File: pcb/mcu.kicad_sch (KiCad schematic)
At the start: 6 parts, among them U1 STM32G0B1RET6

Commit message: fix CAN tx/rx/stb, remove unused SWO
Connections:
- net RX: now also U1.51 (PD1); no longer U1.41 (PD9)
- net STB: now also U1.52 (PD2)
- net TX: now also U1.50 (PD0); no longer U1.40 (PD8)
- net MCU_STATUS_LED: now reaches U1.13 (PC0)
- no-connect marks 38 -> 37
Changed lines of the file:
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@@
+	)
+	(no_connect
+		(at 137.16 104.14)
 	)
 	(no_connect
@@
 	)
 	(no_connect
-		(at 81.28 106.68)
-	)
-	(no_connect
 		(at 137.16 129.54)
 	)
@@
 	(no_connect
 		(at 137.16 121.92)
-	)
-	(no_connect
-		(at 81.28 86.36)
 	)
 	(no_connect
@@
 	)
 	(bus_entry
+		(at 44.45 83.82)
+		(size 2.54 2.54)
+		(stroke
+			(width 0)
+			(type default)
+		)
+	)
+	(bus_entry
 		(at 191.77 62.23)
 		(size -2.54 2.54)
@@
 	)
 	(bus_entry
-		(at 53.34 95.25)
-		(size 2.54 2.54)
-		(stroke
-			(width 0)
-			(type default)
-		)
-	)
-	(bus_entry
-		(at 53.34 105.41)
-		(size 2.54 2.54)
-		(stroke
-			(width 0)
-			(type default)
-		)
-	)
-	(bus_entry
 		(at 191.77 69.85)
 		(size -2.54 2.54)
@@
 	)
 	(bus_entry
-		(at 53.34 97.79)
+		(at 44.45 81.28)
 		(size 2.54 2.54)
 		(stroke
@@
 		)
 	)
+	(bus_entry
+		(at 44.45 78.74)
+		(size 2.54 2.54)
+		(stroke
+			(width 0)
+			(type default)
+		)
+	)
 	(wire
 		(pts
@@
 	(wire
 		(pts
+			(xy 77.47 106.68) (xy 81.28 106.68)
+		)
+		(stroke
+			(width 0)
+			(type default)
+		)
+	)
+	(bus
+		(pts
+			(xy 44.45 81.28) (xy 44.45 83.82)
+		)
+		(stroke
+			(width 0)
+			(type default)
+		)
+	)
+	(bus
+		(pts
+			(xy 44.45 68.58) (xy 44.45 78.74)
+		)
+		(stroke
+			(width 0)
+			(type default)
+		)
+	)
+	(wire
+		(pts
 			(xy 137.16 66.04) (xy 156.21 66.04)
 		)
@@
 	(wire
 		(pts
-			(xy 76.2 101.6) (xy 81.28 101.6)
-		)
-		(stroke
-			(width 0)
-			(type default)
-		)
-	)
-	(wire
-		(pts
 			(xy 55.88 116.84) (xy 81.28 116.84)
 		)
@@
 	(wire
 		(pts
+			(xy 46.99 81.28) (xy 81.28 81.28)
+		)
+		(stroke
+			(width 0)
+			(type default)
+		)
+	)
+	(wire
+		(pts
 			(xy 172.72 67.31) (xy 189.23 67.31)
 		)
@@
 		)
 	)
-	(bus
-		(pts
-			(xy 53.34 85.09) (xy 53.34 95.25)
-		)
-		(stroke
-			(width 0)
-			(type default)
-		)
-	)
-	(wire
-		(pts
-			(xy 76.2 97.79) (xy 77.47 99.06)
-		)
-		(stroke
-			(width 0)
-			(type default)
-		)
-	)
 	(wire
 		(pts
@@
 	(wire
 		(pts
-			(xy 55.88 97.79) (xy 76.2 97.79)
-		)
-		(stroke
-			(width 0)
-			(type default)
-		)
-	)
-	(bus
-		(pts
-			(xy 53.34 95.25) (xy 53.34 97.79)
-		)
-		(stroke
-			(width 0)
-			(type default)
-		)
-	)
-	(wire
-		(pts
 			(xy 137.16 76.2) (xy 156.21 76.2)
 		)
@@
 		)
 	)
-	(wire
-		(pts
-			(xy 77.47 99.06) (xy 81.28 99.06)
-		)
-		(stroke
-			(width 0)
-			(type default)
-		)
-	)
 	(bus
 		(pts
@@
 	(wire
 		(pts
+			(xy 46.99 86.36) (xy 81.28 86.36)
+		)
+		(stroke
+			(width 0)
+			(type default)
+		)
+	)
+	(wire
+		(pts
 			(xy 151.13 88.9) (xy 153.67 91.44)
 		)
@@
 		)
 	)
-	(wire
-		(pts
-			(xy 55.88 107.95) (xy 62.23 107.95)
+	(bus
+		(pts
+			(xy 44.45 78.74) (xy 44.45 81.28)
 		)
 		(stroke
@@
 	(wire
 		(pts
-			(xy 74.93 100.33) (xy 76.2 101.6)
-		)
-		(stroke
-			(width 0)
-			(type default)
-		)
-	)
-	(wire
-		(pts
 			(xy 87.63 50.8) (xy 92.71 50.8)
 		)
@@
 	(wire
 		(pts
+			(xy 46.99 83.82) (xy 81.28 83.82)
+		)
+		(stroke
+			(width 0)
+			(type default)
+		)
+	)
+	(wire
+		(pts
 			(xy 139.7 101.6) (xy 137.16 101.6)
 		)
@@
 	(bus
 		(pts
-			(xy 53.34 97.79) (xy 53.34 105.41)
-		)
-		(stroke
-			(width 0)
-			(type default)
-		)
-	)
-	(bus
-		(pts
 			(xy 165.1 87.63) (xy 165.1 88.9)
-		)
-		(stroke
-			(width 0)
-			(type default)
-		)
-	)
-	(wire
-		(pts
-			(xy 55.88 100.33) (xy 74.93 100.33)
 		)
 		(stroke
@@
 		)
 	)
+	(label "STB"
+		(at 46.99 86.36 0)
+		(effects
+			(font
+				(size 1.27 1.27)
+			)
+			(justify left bottom)
+		)
+	)
 	(label "DBG_UART.RX"
 		(at 161.29 137.16 180)
@@
 		)
 	)
+	(label "RX"
+		(at 46.99 83.82 0)
+		(effects
+			(font
+				(size 1.27 1.27)
+			)
+			(justify left bottom)
+		)
+	)
 	(label "HLINE.RX"
 		(at 172.72 83.82 0)
@@
 		)
 	)
-	(label "STB"
-		(at 55.88 107.95 0)
-		(effects
-			(font
-				(size 1.27 1.27)
-			)
-			(justify left bottom)
-		)
-	)
-	(label "TX"
-		(at 55.88 97.79 0)
-		(effects
-			(font
-				(size 1.27 1.27)
-			)
-			(justify left bottom)
-		)
-	)
 	(label "KLINE.TX"
 		(at 67.31 116.84 180)
@@
 		)
 	)
-	(label "RX"
-		(at 55.88 100.33 0)
+	(label "TX"
+		(at 46.99 81.28 0)
 		(effects
 			(font
@@
 		)
 	)
-	(hierarchical_label "MCU_SWO"
+	(hierarchical_label "MCU_STATUS_LED"
 		(shape output)
-		(at 139.7 104.14 0)
+		(at 77.47 106.68 180)
+		(effects
+			(font
+				(size 1.27 1.27)
+			)
+			(justify right)
+		)
+	)
+	(hierarchical_label "{CAN_MCU}"
+		(shape bidirectional)
+		(at 44.45 68.58 0)
 		(effects
 			(font
@@
 		)
 	)
-	(hierarchical_label "{CAN_MCU}"
-		(shape bidirectional)
-		(at 53.34 85.09 0)
-		(effects
-			(font
-				(size 1.27 1.27)
-			)
-			(justify left)
-		)
-	)

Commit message: status/info leds, extra 5v cap
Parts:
- renumbered C9 to C20, C10 to C21, C11 to C22, C12 to C23
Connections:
- net MCU_LED_DRV: now reaches U1.38 (PC6)
- no-connect marks 37 -> 38
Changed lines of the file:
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@@
-	)
-	(no_connect
-		(at 81.28 121.92)
 	)
 	(no_connect
@@
 	)
 	(no_connect
+		(at 81.28 101.6)
+	)
+	(no_connect
 		(at 81.28 93.98)
 	)
@@
 	(no_connect
 		(at 137.16 127)
+	)
+	(no_connect
+		(at 81.28 99.06)
 	)
 	(no_connect
@@
 		)
 	)
+	(wire
+		(pts
+			(xy 73.66 121.92) (xy 81.28 121.92)
+		)
+		(stroke
+			(width 0)
+			(type default)
+		)
+	)
 	(bus
 		(pts
@@
 		(shape input)
 		(at 67.31 76.2 180)
+		(effects
+			(font
+				(size 1.27 1.27)
+			)
+			(justify right)
+		)
+	)
+	(hierarchical_label "MCU_LED_DRV"
+		(shape output)
+		(at 73.66 121.92 180)
 		(effects
 			(font
@@
 		(on_board yes)
 		(dnp no)
-		(property "Reference" "C12"
+		(property "Reference" "C23"
 			(at 94.488 52.324 0)
 			(effects
@@
 			(project "kh_obd2_interface"
 				(path "/0736e313-8db4-41af-b70d-53af7104d2ca/c18d60e7-bd36-4ea9-b2f1-adbb43a4c5ec"
-					(reference "C12")
+					(reference "C23")
 					(unit 1)
 				)
@@
 		(on_board yes)
 		(dnp no)
-		(property "Reference" "C10"
+		(property "Reference" "C21"
 			(at 127.508 52.324 0)
 			(effects
@@
 			(project "kh_obd2_interface"
 				(path "/0736e313-8db4-41af-b70d-53af7104d2ca/c18d60e7-bd36-4ea9-b2f1-adbb43a4c5ec"
-					(reference "C10")
+					(reference "C21")
 					(unit 1)
 				)
@@
 		(on_board yes)
 		(dnp no)
-		(property "Reference" "C11"
+		(property "Reference" "C22"
 			(at 84.328 52.324 0)
 			(effects
@@
 			(project ""
 				(path "/0736e313-8db4-41af-b70d-53af7104d2ca/c18d60e7-bd36-4ea9-b2f1-adbb43a4c5ec"
-					(reference "C11")
+					(reference "C22")
 					(unit 1)
 				)
@@
 		(on_board yes)
 		(dnp no)
-		(property "Reference" "C9"
+		(property "Reference" "C20"
 			(at 117.348 52.324 0)
 			(effects
@@
 			(project ""
 				(path "/0736e313-8db4-41af-b70d-53af7104d2ca/c18d60e7-bd36-4ea9-b2f1-adbb43a4c5ec"
-					(reference "C9")
+					(reference "C20")
 					(unit 1)
 				)

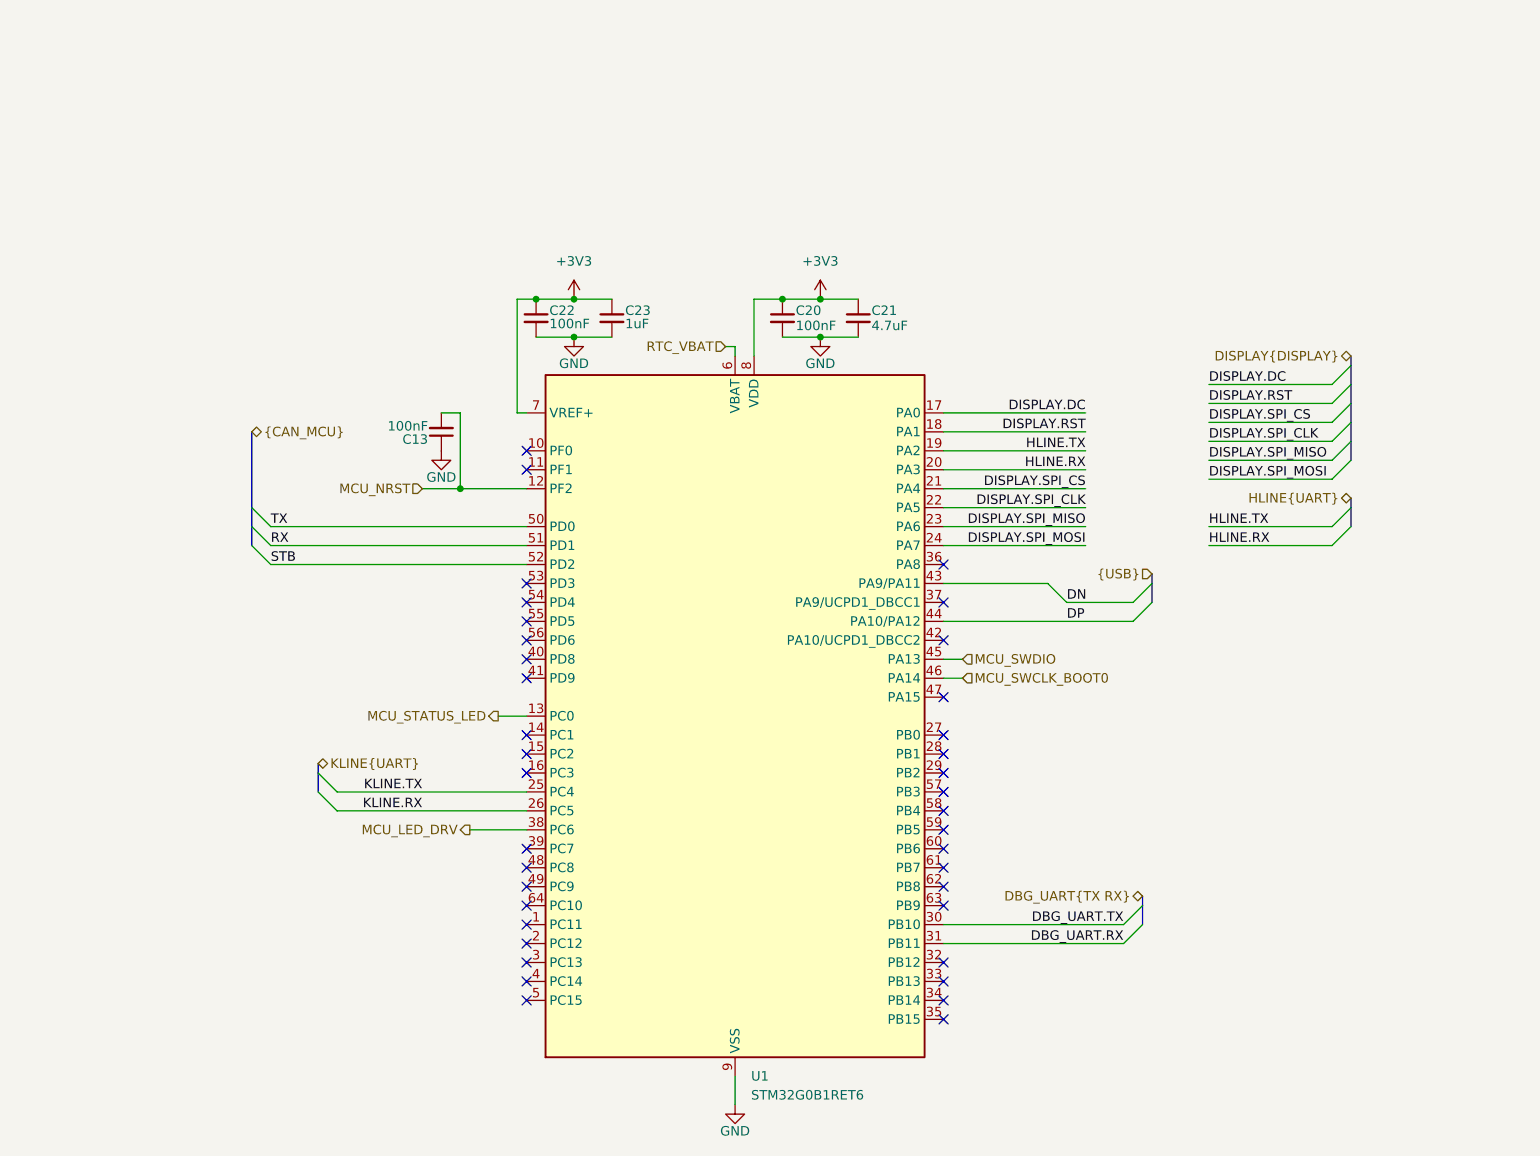
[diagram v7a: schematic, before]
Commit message: dbg uart, nrst, SCS drive, etc
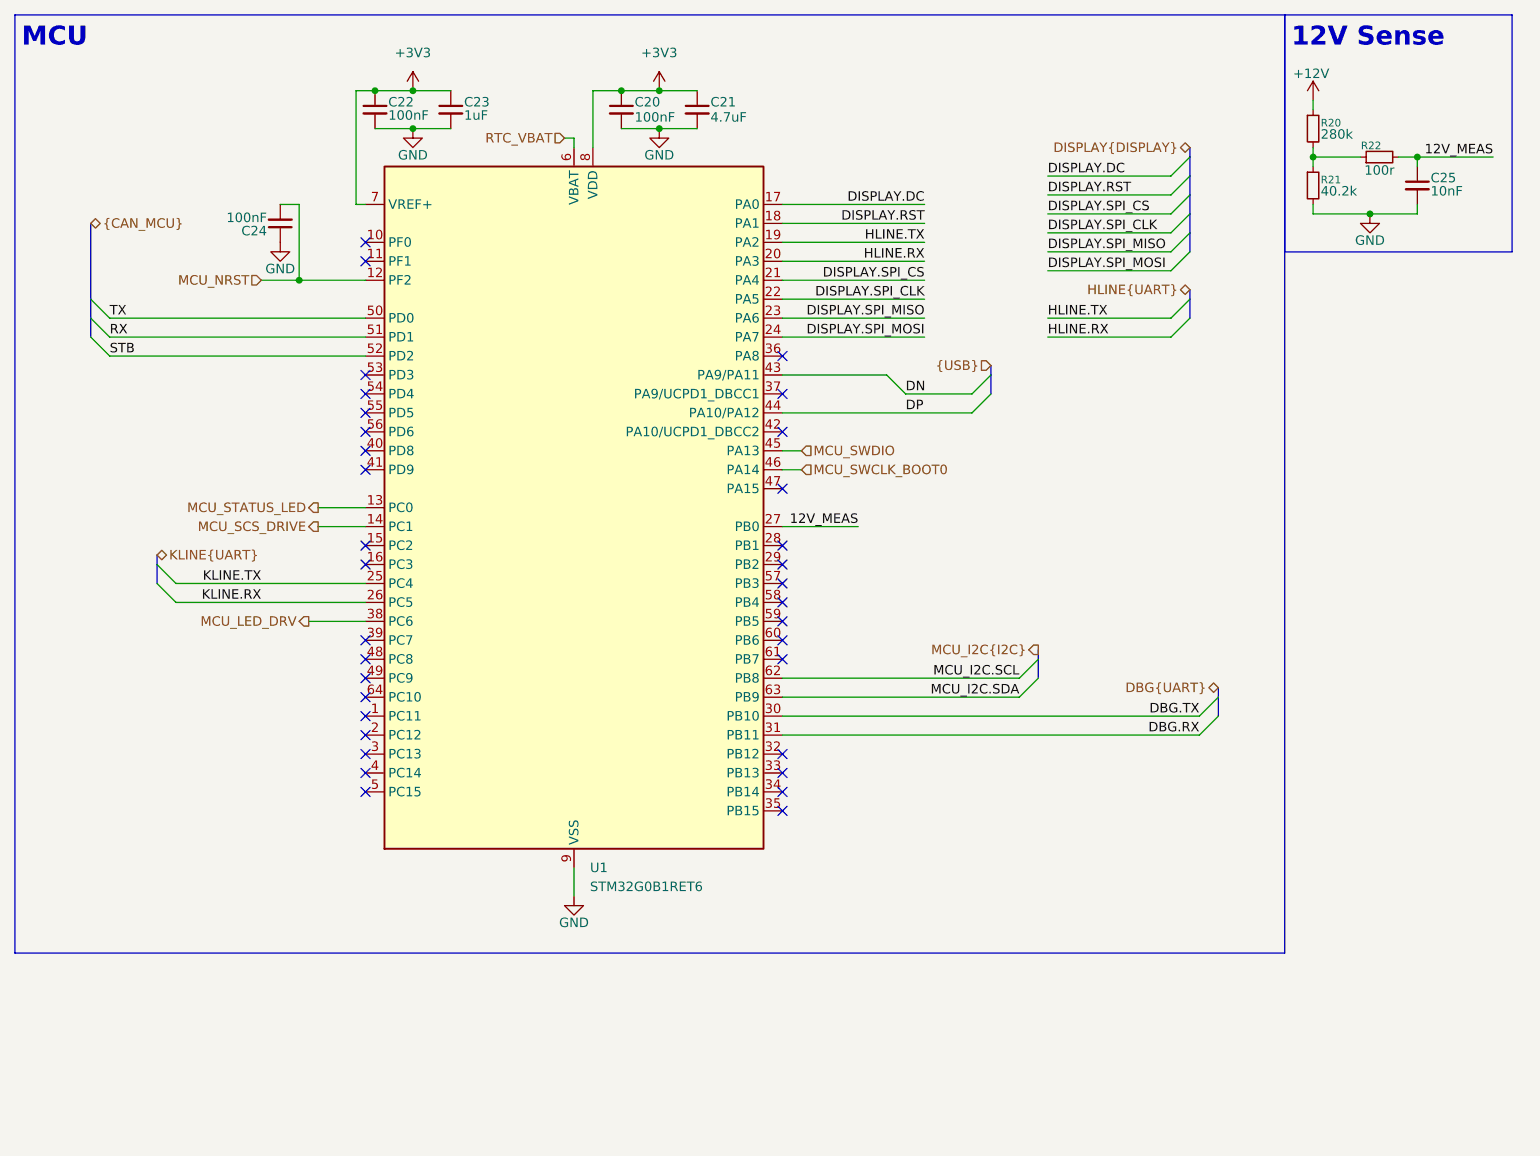
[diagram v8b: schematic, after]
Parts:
- added C25: 10nF, Capacitor_SMD:C_0402_1005Metric, symbol Device:C_Small
- added R20: 280k, Resistor_SMD:R_0402_1005Metric, symbol Device:R_Small
- added R21: 40.2k, Resistor_SMD:R_0402_1005Metric, symbol Device:R_Small
- added R22: 100r, Resistor_SMD:R_0402_1005Metric, symbol Device:R_Small
- renumbered C13 to C24
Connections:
- net GND: now also C25.2, R21.2
- net MCU_SCS_DRIVE: now reaches U1.14 (PC1)
- net 12V_MEAS: now reaches U1.27 (PB0)
- net 12V_MEAS: now also C25.1, R22.2
- net MCU_I2C.SCL: now reaches U1.62 (PB8)
- net MCU_I2C.SDA: now reaches U1.63 (PB9)
- net DBG_UART.RX renamed DBG.RX
- net DBG_UART.TX renamed DBG.TX
- new net: R20.2, R21.1, R22.1
- new net +12V: R20.1
- no-connect marks 38 -> 34
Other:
- note added: "12V Sense"
- note added: "MCU"
- moved on the sheet: C20, C21, C22, C23, C24, U1
